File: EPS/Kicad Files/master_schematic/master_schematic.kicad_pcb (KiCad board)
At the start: 2 copper layers, 96 x 90 mm, 5 parts, among them J1 THD-20-R

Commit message: EPS master netlist complete
dropped all parts onto pcb
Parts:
- added C1: 20μF, Capacitor_SMD:C_0603_1608Metric, F.Cu at (249.9, 42.2)
- added C10: 10uF, Capacitor_SMD:C_0603_1608Metric, F.Cu at (70.1, 66.5)
- added C11: 10uF, Capacitor_SMD:C_0603_1608Metric, F.Cu at (65.5, 64.0)
- added C12: 10uF, Capacitor_SMD:C_0603_1608Metric, F.Cu at (68.3, 66.5)
- added C13: 22uF, Capacitor_SMD:C_0603_1608Metric, F.Cu at (65.5, 62.2)
- added C14: 0.1uF, Capacitor_SMD:C_0603_1608Metric, F.Cu at (161.1, 76.3)
- added C15: 0.47uF, Capacitor_SMD:C_0603_1608Metric, F.Cu at (169.2, 94.0)
- added C16: 100nF, Capacitor_SMD:C_0603_1608Metric, F.Cu at (203.2, 19.3)
- added C17: 4.7nF, Capacitor_SMD:C_0603_1608Metric, F.Cu at (198.6, 101.6)
- added C18: 0.1uF, Capacitor_SMD:C_0603_1608Metric, F.Cu at (189.7, 45.7)
- added C19: 0.1uF, Capacitor_SMD:C_0603_1608Metric, F.Cu at (193.7, 45.7)
- added C2: 20μF, Capacitor_SMD:C_0603_1608Metric, F.Cu at (212.4, 77.9)
- added C20: 22uF, Capacitor_SMD:C_0603_1608Metric, F.Cu at (194.0, 42.2)
- added C21: 0.1uF, Capacitor_SMD:C_0603_1608Metric, F.Cu at (183.0, 102.2)
- added C3: 20μF, Capacitor_SMD:C_0603_1608Metric, F.Cu at (222.5, 49.8)
- added C4: 0.1μF, Capacitor_SMD:C_0402_1005Metric, F.Cu at (253.4, 41.9)
- added C5: 2.2uF, Capacitor_SMD:C_0603_1608Metric, F.Cu at (62.0, 64.3)
- added C6: 2.2uF, Capacitor_SMD:C_0603_1608Metric, F.Cu at (64.0, 71.1)
- added C7: 2.2uF, Capacitor_SMD:C_0603_1608Metric, F.Cu at (72.1, 66.5)
- added C8: 10uF, Capacitor_SMD:C_0603_1608Metric, F.Cu at (68.3, 69.8)
- added C9: 0.1uF, Capacitor_SMD:C_0402_1005Metric, F.Cu at (67.6, 63.2)
- added CR1: BZX884B5V1L-HG3-08, hg3-08:BZX884B5V1L-HG3-08, F.Cu at (251.0, 68.1)
- added D1: LED, LED_SMD:LED_0603_1608Metric, F.Cu at (117.6, 40.6)
- added D2: LED, LED_SMD:LED_0603_1608Metric, F.Cu at (117.9, 32.5)
- added D3: DIODE, Diode_SMD:D_0805_2012Metric, F.Cu at (162.6, 39.6)
- added D4: PD3Z284C3V6-7, PD3z284:PD3Z284C3V6-7, F.Cu at (263.6, 46.6)
- added D5: RED, LED_SMD:LED_0603_1608Metric, F.Cu at (131.3, 30.0)
- added D6: GREEN, LED_SMD:LED_0603_1608Metric, F.Cu at (131.1, 37.6)
- added D7: YELLOW, LED_SMD:LED_0603_1608Metric, F.Cu at (131.1, 41.1)
- added D8: YELLOW, LED_SMD:LED_0603_1608Metric, F.Cu at (118.4, 109.2)
- added D9: YELLOW, LED_SMD:LED_0603_1608Metric, F.Cu at (131.1, 47.8)
- added J2: 436500212, molex connector:436500212, F.Cu at (50.5, 93.7)
- added J3: Conn_02x20_Odd_Even, Connector_PinHeader_2.54mm:PinHeader_2x20_P2.54mm_Vertical, F.Cu at (128.4, 76.8)
- added J4: Conn_01x05_Female, Connector_PinSocket_2.54mm:PinSocket_1x05_P2.54mm_Vertical, F.Cu at (122.5, 15.3)
- added JP1: SolderJumper_2_Open, Jumper:SolderJumper-2_P1.3mm_Bridged2Bar_Pad1.0x1.5mm, F.Cu at (189.8, 42.7)
- added L1: .47uH, Inductor_SMD:L_1008_2520Metric, F.Cu at (70.9, 62.7)
- added Q1: FZT688BTA, fzt:SOT230P700X180-4N, F.Cu at (262.1, 80.8)
- added Q2: FZT688BTA, fzt:SOT230P700X180-4N, F.Cu at (261.8, 67.6)
- added R1: PSF4NTEBL500F, psf4nt:PSF4NTEBL500F, F.Cu at (222.0, 19.7)
- added R10: 1k, Resistor_SMD:R_0402_1005Metric, F.Cu at (56.6, 78.7)
- added R11: 10k, Resistor_SMD:R_0402_1005Metric, F.Cu at (63.8, 80.3)
- added R12: 0.010, Resistor_SMD:R_0805_2012Metric, F.Cu at (100.6, 49.0)
- added R13: 60, Resistor_SMD:R_0603_1608Metric, F.Cu at (191.5, 18.8)
- added R14: 60, Resistor_SMD:R_0603_1608Metric, F.Cu at (199.3, 109.5)
- added R15: 10k, Resistor_SMD:R_0603_1608Metric, F.Cu at (179.6, 82.1)
- added R16: 200, Resistor_SMD:R_0603_1608Metric, F.Cu at (107.7, 19.8)
- added R17: 1k, Resistor_SMD:R_0603_1608Metric, F.Cu at (255.0, 68.1)
- added R18: 1k, Resistor_SMD:R_0603_1608Metric, F.Cu at (255.0, 73.2)
- added R19: 330, Resistor_SMD:R_0603_1608Metric, F.Cu at (124.1, 50.3)
- added R2: PSF4NTEBL500F, psf4nt:PSF4NTEBL500F, F.Cu at (219.2, 57.5)
- added R20: 330, Resistor_SMD:R_0603_1608Metric, F.Cu at (118.3, 114.4)
- added R21: 330, Resistor_SMD:R_0603_1608Metric, F.Cu at (124.3, 41.1)
- added R22: 330, Resistor_SMD:R_0603_1608Metric, F.Cu at (187.0, 99.7)
- added R23: 330, Resistor_SMD:R_0603_1608Metric, F.Cu at (191.1, 97.1)
- added R3: 10kΩ, Resistor_SMD:R_0603_1608Metric, F.Cu at (249.9, 44.7)
- added R4: 10kΩ, Resistor_SMD:R_0603_1608Metric, F.Cu at (212.4, 80.4)
- added R5: 10kΩ, Resistor_SMD:R_0603_1608Metric, F.Cu at (216.4, 77.9)
- added R6: 10kΩ, Resistor_SMD:R_0603_1608Metric, F.Cu at (227.6, 72.7)
- added R7: 10kΩ, Resistor_SMD:R_0603_1608Metric, F.Cu at (234.7, 44.2)
- added R8: 1k, Resistor_SMD:R_0402_1005Metric, F.Cu at (56.4, 81.5)
- added R9: 24.9k, Resistor_SMD:R_0402_1005Metric, F.Cu at (56.4, 84.3)
- added Rpu1: 10kΩ, Resistor_SMD:R_0603_1608Metric, F.Cu at (239.8, 44.2)
- added TH1: 10k, Resistor_SMD:R_0603_1608Metric, F.Cu at (67.6, 80.5)
- added U1: RPM5.0-2.0, Converter_DCDC:Converter_DCDC_RECOM_RPMx.x-x.0, F.Cu at (92.5, 69.6)
- added U2: RPM5.0-2.0, Converter_DCDC:Converter_DCDC_RECOM_RPMx.x-x.0, F.Cu at (109.7, 69.6)
- added U3: RPM3.3-2.0, Converter_DCDC:Converter_DCDC_RECOM_RPMx.x-x.0, F.Cu at (109.7, 87.9)
- added U4: INA3221, Package_DFN_QFN:Texas_RGV_S-PVQFN-N16_EP2.1x2.1mm, F.Cu at (222.5, 32.5)
- added U5: MAX77757JEFG435+, max77757:IC_MAX77757JEFG435+, F.Cu at (64.5, 67.6)
- added U6: MAX17055EWL+T, max17055:MAX17055EWL_plus_T, F.Cu at (71.9, 83.3)
- added U7: ATA6560-GAQW-VAO, ata6560:ATA6560-GAQW-VAO, F.Cu at (95.5, 121.4)
- added U8: PIC18F27Q84-E/SP, pic18f27:PIC18F27Q84-E&slash_SP, F.Cu at (64.0, 137.9)
- J1: value THD-20-R -> USB_C_Receptacle; footprint Connector_PinHeader_2.54mm:PinHeader_2x20_P2.54mm_Vertical -> Connector_USB:USB_C_Receptacle_Amphenol_12401610E4-2A
- moved J1 84.3 mm to (44.2, 72.6), turned to -90 degrees
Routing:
- net /ColoradoCUBE_Payload/5V: track 0.00 -> 1.13 mm
- net (no net): track 1.13 -> 0.00 mm

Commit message: pcb update
progress on pcb layout
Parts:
- moved C16 174.6 mm to (58.4, 116.8), turned to 90 degrees
- moved R3 170.7 mm to (99.1, 124.5), turned to -90 degrees
- moved C4 169.6 mm to (106.7, 127.0), turned to -90 degrees
- moved JP1 167.5 mm to (53.3, 139.7), turned to -90 degrees
- moved D4 163.8 mm to (109.2, 101.6), turned to -90 degrees
- moved C18 162.9 mm to (58.4, 142.2), turned to 180 degrees
- moved C20 159.3 mm to (53.3, 116.8), turned to -90 degrees
- moved Q2 150.1 mm to (116.8, 106.7)
- moved R18 149.6 mm to (109.2, 106.7), turned to -90 degrees
- moved C1 147.7 mm to (104.1, 66.0), turned to -90 degrees
- moved R17 147.3 mm to (109.2, 88.9), turned to -90 degrees
- moved Q1 145.3 mm to (116.8, 81.3)
- moved R13 143.9 mm to (83.8, 114.3), turned to -90 degrees
- moved U4 143.7 mm to (114.3, 127.0)
- moved CR1 142.3 mm to (109.2, 81.3), turned to -90 degrees
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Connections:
- Q1 pad 1: GND -> Net-(CR1-Pad2)
- Q1 pad 2: Net-(CR1-Pad2) -> (no net)
- Q1 pad 3: /ColoradoCUBE_Payload/5V -> GND
- Q1 pad 4: (no net) -> /ColoradoCUBE_Payload/5V
- Q2 pad 1: GND -> Net-(D4-Pad2)
- Q2 pad 2: Net-(D4-Pad2) -> (no net)
- Q2 pad 3: /ColoradoCUBE_Payload/3.3V -> GND
- Q2 pad 4: (no net) -> /ColoradoCUBE_Payload/3.3V
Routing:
- net GND: track 0.00 -> 377.1 mm, vias 0 -> 5
- net /ColoradoCUBE_Payload/5V: track 1.13 -> 295.4 mm, vias 0 -> 4
- net /ColoradoCUBE_Payload/3.3V: track 0.00 -> 131.9 mm, vias 0 -> 1
- net Net-(R2-Pad3): track 0.00 -> 92.5 mm, vias 0 -> 2
- net /ColoradoCUBE_Payload/CANL: track 0.00 -> 91.0 mm, vias 0 -> 1
- net /ColoradoCUBE_Payload/CANH: track 0.00 -> 86.5 mm, vias 0 -> 3
- net Net-(R2-Pad2): track 0.00 -> 75.5 mm, vias 0 -> 2
- net Net-(C1-Pad1): track 0.00 -> 62.9 mm
- net Net-(R1-Pad3): track 0.00 -> 45.0 mm, vias 0 -> 2
- net Net-(R1-Pad2): track 0.00 -> 41.4 mm, vias 0 -> 2
- net /ColoradoCUBE_Payload/MCLR: track 0.00 -> 34.1 mm
- net /ColoradoCUBE_Payload/ICSPC: track 0.00 -> 34.0 mm, vias 0 -> 1
- net /ColoradoCUBE_Payload/ICSPD: track 0.00 -> 28.8 mm, vias 0 -> 1
- net Net-(C3-Pad1): track 0.00 -> 28.7 mm
- net /ColoradoCUBE_Payload/CAN_Transceiver/PWR: track 0.00 -> 22.5 mm
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
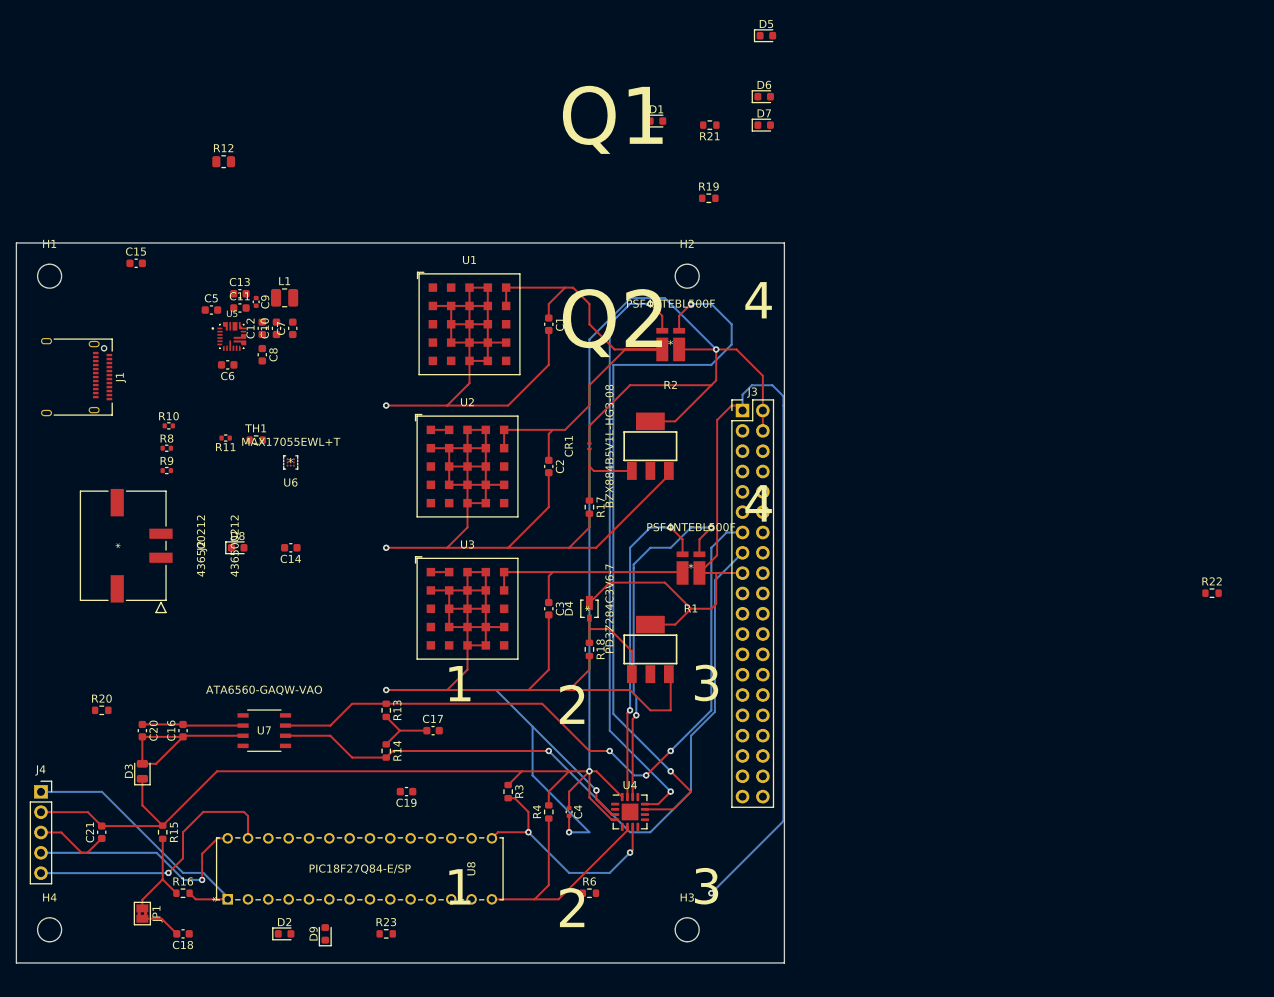
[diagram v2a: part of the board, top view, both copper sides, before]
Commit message: updated pcb layout
last thing needed is the charger schematic
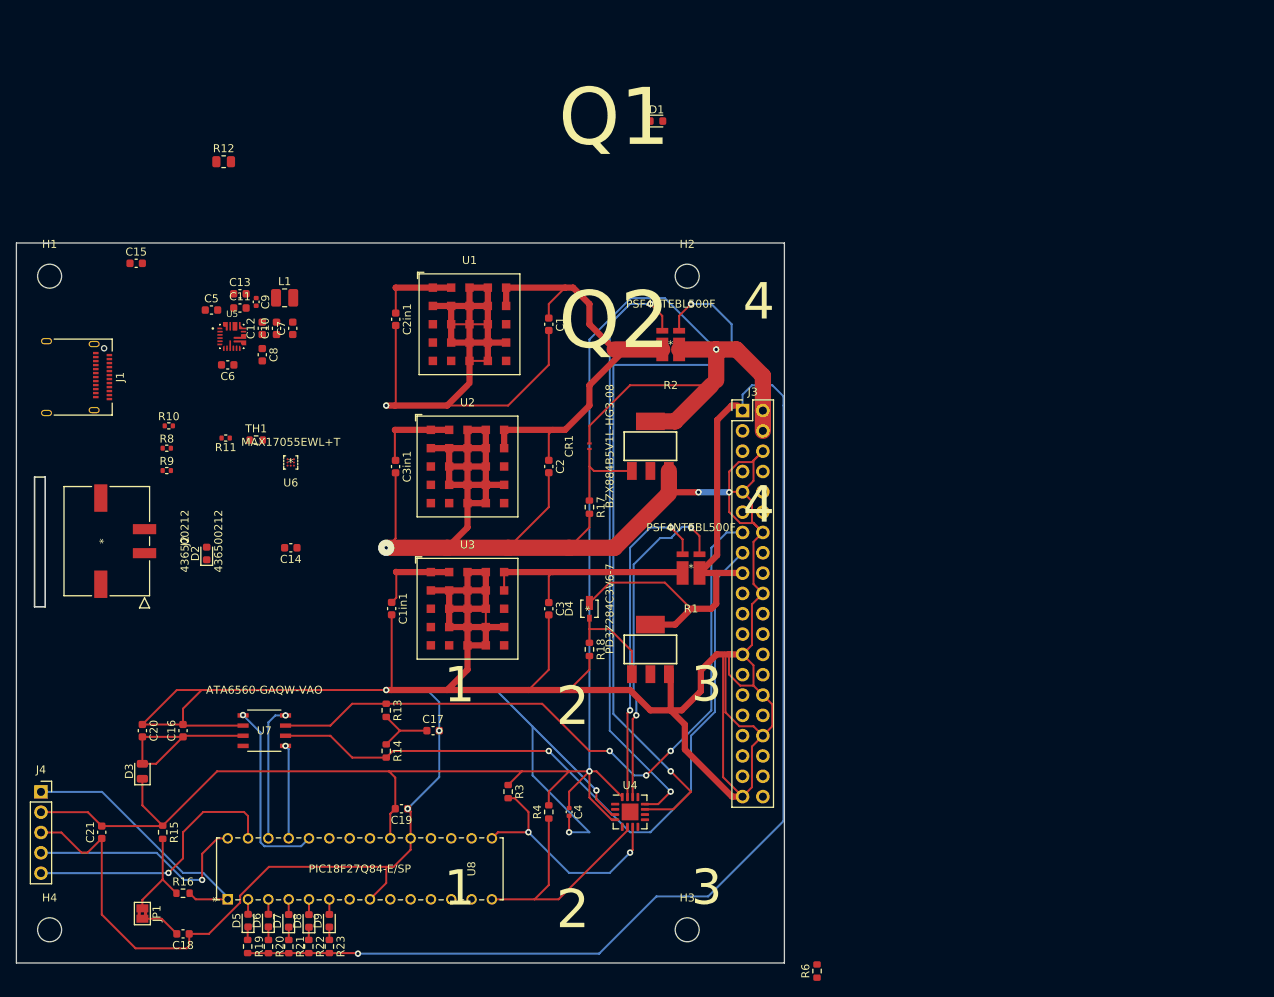
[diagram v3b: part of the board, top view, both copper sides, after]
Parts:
- added C1in1: 20μF, Capacitor_SMD:C_0603_1608Metric, F.Cu at (84.5, 101.6)
- added C2in1: 20μF, Capacitor_SMD:C_0603_1608Metric, F.Cu at (85.0, 65.4)
- added C3in1: 20μF, Capacitor_SMD:C_0603_1608Metric, F.Cu at (85.0, 83.8)
- moved D5 128.2 mm to (66.5, 140.6), turned to 90 degrees
- moved R22 121.2 mm to (74.1, 143.8), turned to -90 degrees
- moved D6 120.2 mm to (69.1, 140.6), turned to 90 degrees
- moved D7 115.9 mm to (71.6, 140.6), turned to 90 degrees
- moved R21 115.4 mm to (71.6, 143.8), turned to -90 degrees
- moved R19 109.9 mm to (66.5, 143.8), turned to -90 degrees
- moved D2 48.5 mm to (61.4, 94.7), turned to 90 degrees
- moved D8 47.5 mm to (74.2, 140.6), turned to 90 degrees
- moved R20 36.1 mm to (69.1, 143.8), turned to -90 degrees
- moved R6 30.1 mm to (137.7, 146.9), turned to 90 degrees
- moved R23 7.28 mm to (76.7, 143.8), turned to -90 degrees
- moved C19 2.23 mm to (85.7, 126.6)
- moved J2 2.14 mm to (48.5, 93.2)
- moved D9 1.72 mm to (76.7, 140.6)
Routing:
- net GND: track 377.1 -> 671.8 mm, vias 5 -> 9
- net /ColoradoCUBE_Payload/3.3V: track 131.9 -> 193.0 mm
- net /charge schem/SYSPOWER: track 4.58 -> 31.5 mm
- net /ColoradoCUBE_Payload/CAN_Transceiver/CAN_TX: track 0.00 -> 23.5 mm, vias 0 -> 1
- net /ColoradoCUBE_Payload/CAN_Transceiver/STBY: track 0.00 -> 17.0 mm, vias 0 -> 1
- net /ColoradoCUBE_Payload/CAN_Transceiver/NSIL: track 0.00 -> 11.7 mm, vias 0 -> 1
- net /ColoradoCUBE_Payload/5V: track 295.4 -> 304.4 mm
- net Net-(C1-Pad1): track 62.9 -> 58.2 mm
- net Net-(R1-Pad3): track 45.0 -> 42.4 mm
- net /ColoradoCUBE_Payload/LED_4: track 0.00 -> 1.91 mm
- net /ColoradoCUBE_Payload/LED_3: track 0.00 -> 1.90 mm
- net /ColoradoCUBE_Payload/LED_5: track 0.00 -> 1.89 mm
- net /ColoradoCUBE_Payload/LED_2: track 0.00 -> 1.87 mm
- net /ColoradoCUBE_Payload/LED_1: track 0.00 -> 1.87 mm
- net Net-(D5-Pad1): track 0.00 -> 1.65 mm
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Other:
- outline, holes or cut-outs redrawn

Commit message: EPS board updated
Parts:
- moved D1 70.4 mm to (56.3, 75.4), turned to -90 degrees
- moved R12 44.9 mm to (76.1, 88.8)
- moved C15 30.4 mm to (71.6, 82.1)
- moved D2 19.6 mm to (58.3, 75.4), turned to -90 degrees
- moved R9 16.9 mm to (66.3, 70.6)
- moved R8 9.30 mm to (56.3, 72.2), turned to 90 degrees
- moved R11 8.59 mm to (65.6, 71.9)
- moved TH1 7.44 mm to (65.9, 73.3)
- moved R10 6.65 mm to (58.3, 72.3), turned to 90 degrees
- moved U6 6.15 mm to (65.9, 81.9)
- moved C9 1.14 mm to (68.1, 62.2)
- moved C6 0.90 mm to (63.1, 70.9)
- moved C7 0.76 mm to (72.1, 65.8)
- moved C13 0.58 mm to (65.0, 62.5)
- moved C5 0.57 mm to (62.2, 63.8), turned to 90 degrees
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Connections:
- C5 pad 2: GNDPWR -> GND
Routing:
- net /charge schem/SYSPOWER: track 31.5 -> 60.6 mm
- net Net-(J1-PadB5): track 0.00 -> 24.1 mm
- net Net-(J1-PadA7): track 0.00 -> 15.9 mm
- net Net-(J1-PadA6): track 0.00 -> 15.4 mm
- net Net-(J1-PadA5): track 0.00 -> 15.3 mm
- net Net-(C7-Pad1): track 0.00 -> 12.9 mm, vias 0 -> 2
- net Net-(C5-Pad1): track 0.00 -> 11.7 mm, vias 0 -> 4
- net GNDPWR: track 0.00 -> 9.57 mm
- net Net-(C9-Pad1): track 0.00 -> 9.07 mm, vias 0 -> 2
- net Net-(C9-Pad2): track 0.00 -> 7.93 mm, vias 0 -> 2
- net Net-(R11-Pad2): track 0.00 -> 4.14 mm
- net GND: track 671.8 -> 675.1 mm, vias 9 -> 10
- net /charge schem/V_BAT: track 0.00 -> 2.60 mm
- net Net-(C6-Pad1): track 0.00 -> 2.19 mm
- net Net-(C11-Pad1): track 0.00 -> 1.57 mm
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- added copper zone on B.Cu, net Net-(C5-Pad1)

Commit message: eps updated
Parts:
- J2: moved to B.Cu
- moved J2 12.5 mm to (61.0, 94.3)
- moved J1 0.86 mm to (43.3, 72.6)
- moved C8 0.36 mm to (68.6, 69.6)
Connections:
- R9 pad 2: GNDPWR -> GND
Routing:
- net /charge schem/SYSPOWER: track 60.6 -> 53.3 mm
- net GNDPWR: track 9.57 -> 15.6 mm, vias 0 -> 2
- net Net-(C5-Pad1): track 11.7 -> 17.1 mm, vias 4 -> 5
- net /charge schem/V_BAT: track 2.60 -> 6.96 mm
- net Net-(C7-Pad1): track 12.9 -> 15.9 mm
- net Net-(C9-Pad1): track 9.07 -> 10.2 mm
- net Net-(J1-PadB5): track 24.1 -> 25.0 mm
- net Net-(J1-PadA7): track 15.9 -> 16.7 mm
- net Net-(J1-PadA6): track 15.4 -> 16.2 mm
- net Net-(J1-PadA5): track 15.3 -> 16.2 mm
- net Net-(R8-Pad2): track 0.00 -> 0.56 mm
- net Net-(R10-Pad2): track 0.00 -> 0.56 mm
- net GND: vias 10 -> 11
- net (no net): vias 1 -> 0
- added copper zone on F.Cu, net GNDPWR
